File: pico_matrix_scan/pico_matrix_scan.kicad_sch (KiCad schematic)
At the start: 8 parts, among them SW1 SW_Reed, SW2 SW_Reed, SW3 SW_Reed, SW4 SW_Reed

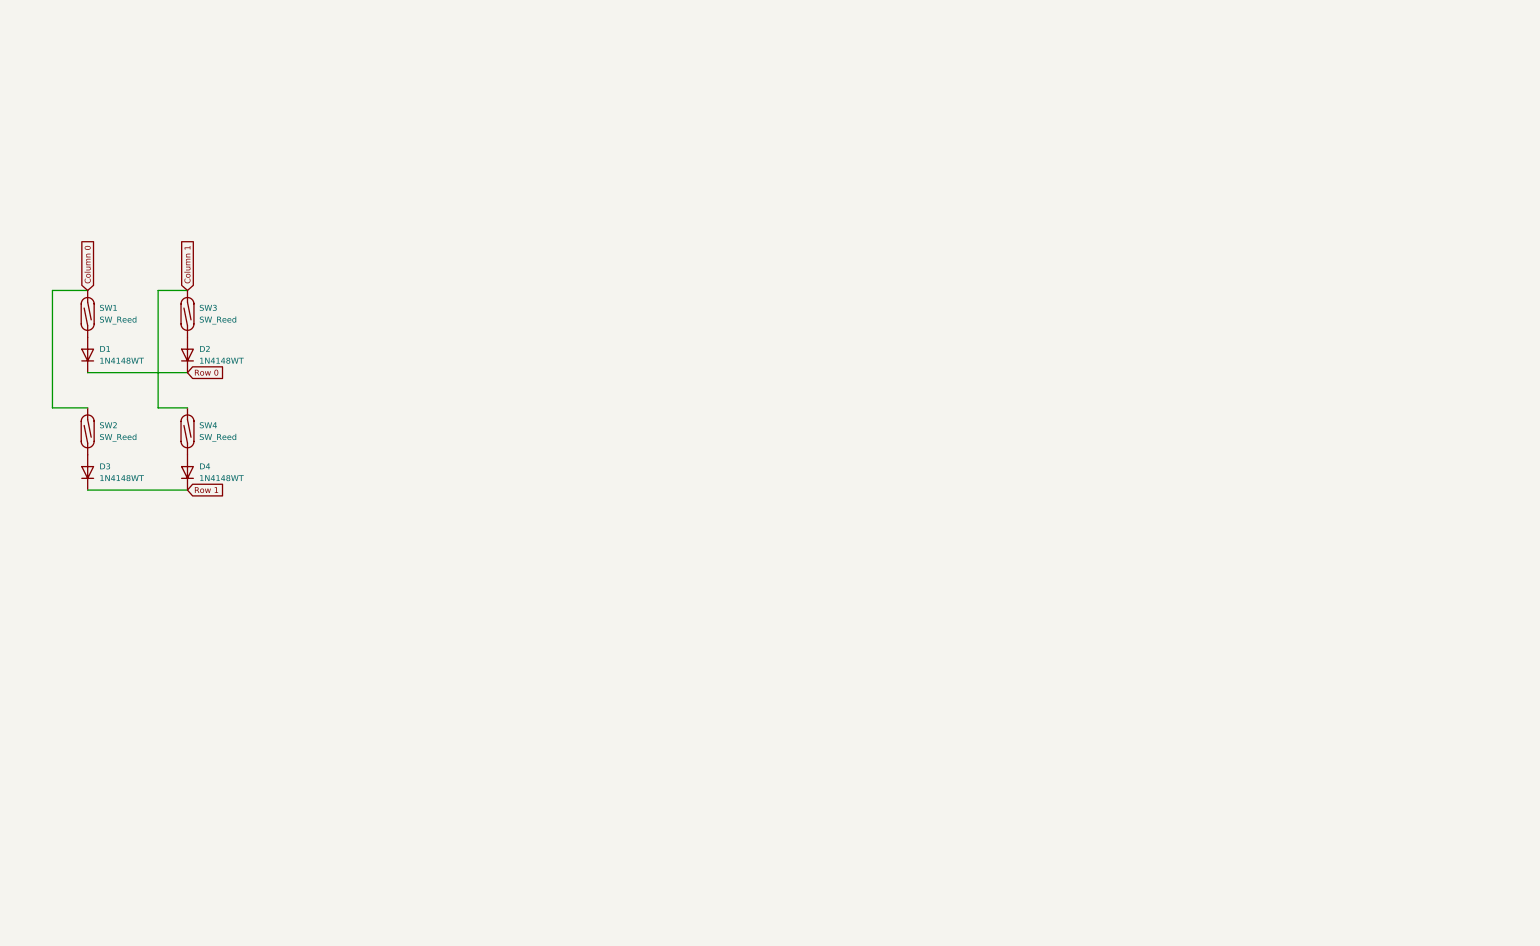
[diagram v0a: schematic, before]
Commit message: Create full-size schematic
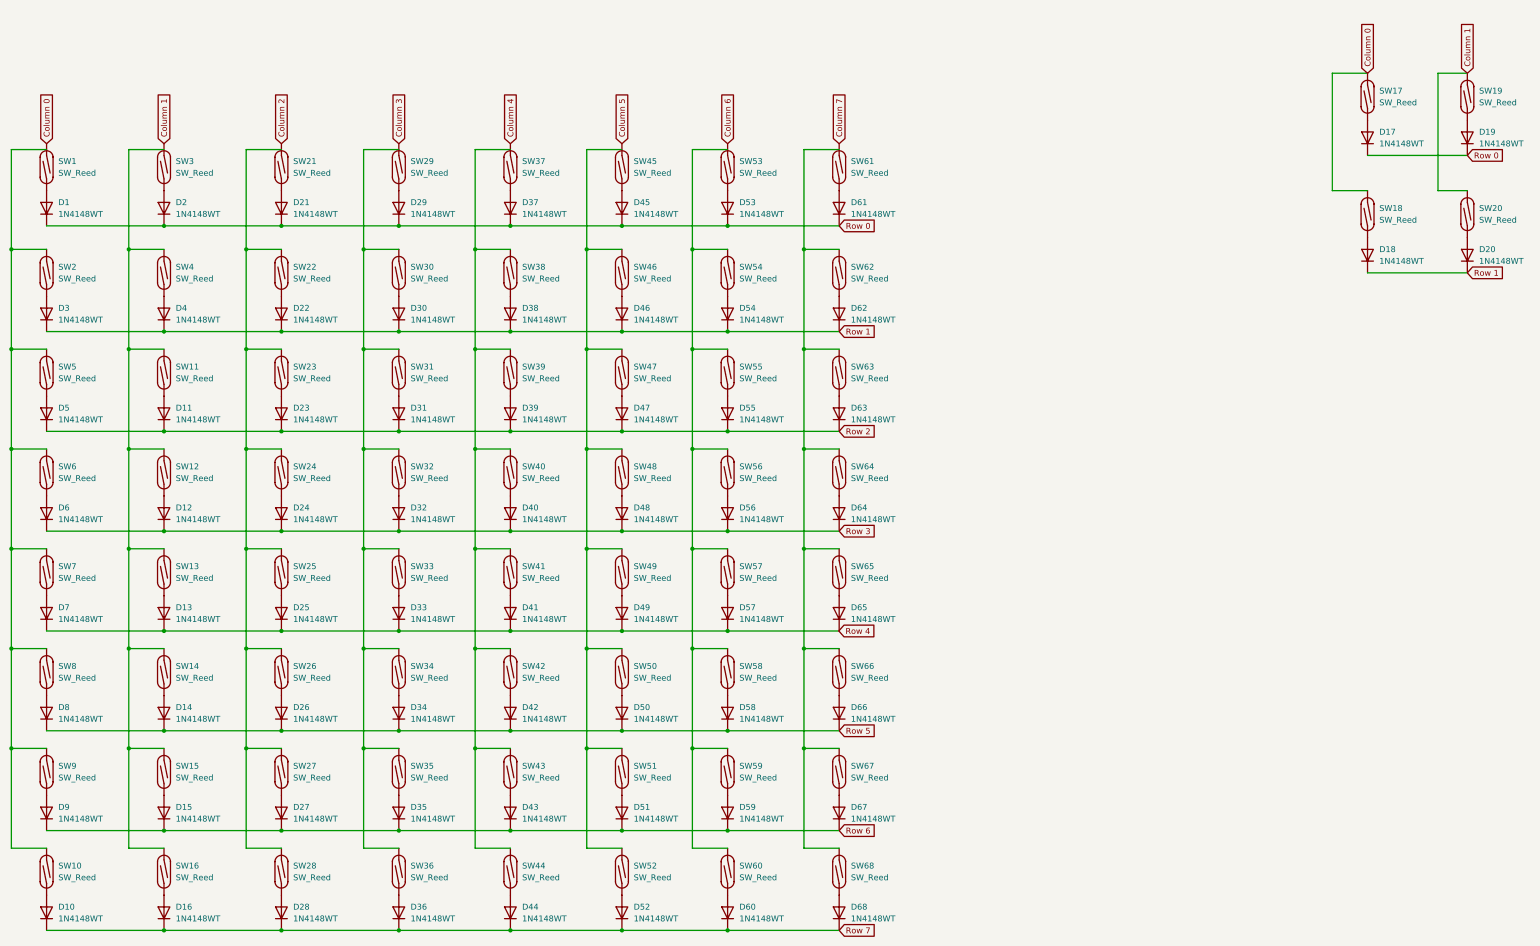
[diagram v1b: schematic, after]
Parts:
- added D10, D11, D12, D13, D14, D15, D16, D17, D18, D19, D20, D21, D22, D23, D24, D25, D26, D27, D28, D29, D30, D31, D32, D33, D34, D35, D36, D37, D38, D39, D40, D41, D42, D43, D44, D45, D46, D47, D48, D49, D5, D50, D51, D52, D53, D54, D55, D56, D57, D58, D59, D6, D60, D61, D62, D63, D64, D65, D66, D67, D68, D7, D8, D9: 1N4148WT, Diode_SMD:D_SOD-523, symbol Diode:1N4148WT
- added SW10, SW11, SW12, SW13, SW14, SW15, SW16, SW17, SW18, SW19, SW20, SW21, SW22, SW23, SW24, SW25, SW26, SW27, SW28, SW29, SW30, SW31, SW32, SW33, SW34, SW35, SW36, SW37, SW38, SW39, SW40, SW41, SW42, SW43, SW44, SW45, SW46, SW47, SW48, SW49, SW5, SW50, SW51, SW52, SW53, SW54, SW55, SW56, SW57, SW58, SW59, SW6, SW60, SW61, SW62, SW63, SW64, SW65, SW66, SW67, SW68, SW7, SW8, SW9: SW_Reed, symbol Switch:SW_Reed
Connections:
- net Column 0: now also SW17.2, SW18.2; no longer SW2.2
- net Column 1: now also SW19.2, SW20.2; no longer SW4.2
- net Row 0: now also D17.1 (K), D19.1 (K), D21.1 (K), D29.1 (K), D37.1 (K), D45.1 (K), D53.1 (K), D61.1 (K)
- net Row 1: now also D18.1 (K), D20.1 (K), D22.1 (K), D30.1 (K), D38.1 (K), D46.1 (K), D54.1 (K), D62.1 (K)
- new net: D45.2 (A), SW45.1
- new net: D9.2 (A), SW9.1
- new net: SW10.2, SW2.2, SW5.2, SW6.2, SW7.2, SW8.2, SW9.2
- new net: D20.2 (A), SW20.1
- new net: D24.2 (A), SW24.1
- new net: D5.2 (A), SW5.1
- new net: D59.2 (A), SW59.1
- new net: D56.2 (A), SW56.1
- new net: SW54.2, SW55.2, SW56.2, SW57.2, SW58.2, SW59.2, SW60.2
- new net: D34.2 (A), SW34.1
- new net: SW30.2, SW31.2, SW32.2, SW33.2, SW34.2, SW35.2, SW36.2
- new net: SW11.2, SW12.2, SW13.2, SW14.2, SW15.2, SW16.2, SW4.2
- new net: D38.2 (A), SW38.1
- new net: SW38.2, SW39.2, SW40.2, SW41.2, SW42.2, SW43.2, SW44.2
- new net: D51.2 (A), SW51.1
- new net: D13.2 (A), SW13.1
- new net: D30.2 (A), SW30.1
- new net: D46.2 (A), SW46.1
- new net: SW46.2, SW47.2, SW48.2, SW49.2, SW50.2, SW51.2, SW52.2
- new net: D63.2 (A), SW63.1
- new net: D25.2 (A), SW25.1
- new net: SW22.2, SW23.2, SW24.2, SW25.2, SW26.2, SW27.2, SW28.2
- new net: D43.2 (A), SW43.1
- new net: D48.2 (A), SW48.1
- new net: D35.2 (A), SW35.1
- new net: D64.2 (A), SW64.1
- new net: SW62.2, SW63.2, SW64.2, SW65.2, SW66.2, SW67.2, SW68.2
- new net: D15.2 (A), SW15.1
- new net: D52.2 (A), SW52.1
- new net: D21.2 (A), SW21.1
- new net: D8.2 (A), SW8.1
- new net: D23.2 (A), SW23.1
- new net: D42.2 (A), SW42.1
- new net: D19.2 (A), SW19.1
- new net: D67.2 (A), SW67.1
- new net: D36.2 (A), SW36.1
- new net: D39.2 (A), SW39.1
- new net: D41.2 (A), SW41.1
- new net: D61.2 (A), SW61.1
- new net: D11.2 (A), SW11.1
- new net: D50.2 (A), SW50.1
- new net: D57.2 (A), SW57.1
- new net: D49.2 (A), SW49.1
- new net: D33.2 (A), SW33.1
- new net: D60.2 (A), SW60.1
- new net: D62.2 (A), SW62.1
- new net: D14.2 (A), SW14.1
- new net: D47.2 (A), SW47.1
- new net: D7.2 (A), SW7.1
- new net: D10.2 (A), SW10.1
- new net: D37.2 (A), SW37.1
- new net: D31.2 (A), SW31.1
- new net: D54.2 (A), SW54.1
- new net: D55.2 (A), SW55.1
- new net: D40.2 (A), SW40.1
- new net: D6.2 (A), SW6.1
- new net: D17.2 (A), SW17.1
- new net: D29.2 (A), SW29.1
- new net: D68.2 (A), SW68.1
- new net: D12.2 (A), SW12.1
- new net: D32.2 (A), SW32.1
- new net: D22.2 (A), SW22.1
- new net: D44.2 (A), SW44.1
- new net: D18.2 (A), SW18.1
- new net: D27.2 (A), SW27.1
- new net: D16.2 (A), SW16.1
- new net: D65.2 (A), SW65.1
- new net: D26.2 (A), SW26.1
- new net: D58.2 (A), SW58.1
- new net: D66.2 (A), SW66.1
- new net: D28.2 (A), SW28.1
- new net: D53.2 (A), SW53.1
- new net Column 2: SW21.2
- new net Column 3: SW29.2
- new net Column 4: SW37.2
- new net Column 5: SW45.2
- new net Column 6: SW53.2
- new net Column 7: SW61.2
- new net Row 2: D11.1 (K), D23.1 (K), D31.1 (K), D39.1 (K), D47.1 (K), D5.1 (K), D55.1 (K), D63.1 (K)
- new net Row 3: D12.1 (K), D24.1 (K), D32.1 (K), D40.1 (K), D48.1 (K), D56.1 (K), D6.1 (K), D64.1 (K)
- new net Row 4: D13.1 (K), D25.1 (K), D33.1 (K), D41.1 (K), D49.1 (K), D57.1 (K), D65.1 (K), D7.1 (K)
- new net Row 5: D14.1 (K), D26.1 (K), D34.1 (K), D42.1 (K), D50.1 (K), D58.1 (K), D66.1 (K), D8.1 (K)
- new net Row 6: D15.1 (K), D27.1 (K), D35.1 (K), D43.1 (K), D51.1 (K), D59.1 (K), D67.1 (K), D9.1 (K)
- new net Row 7: D10.1 (K), D16.1 (K), D28.1 (K), D36.1 (K), D44.1 (K), D52.1 (K), D60.1 (K), D68.1 (K)
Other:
- moved on the sheet: D1, D3, SW1, SW2

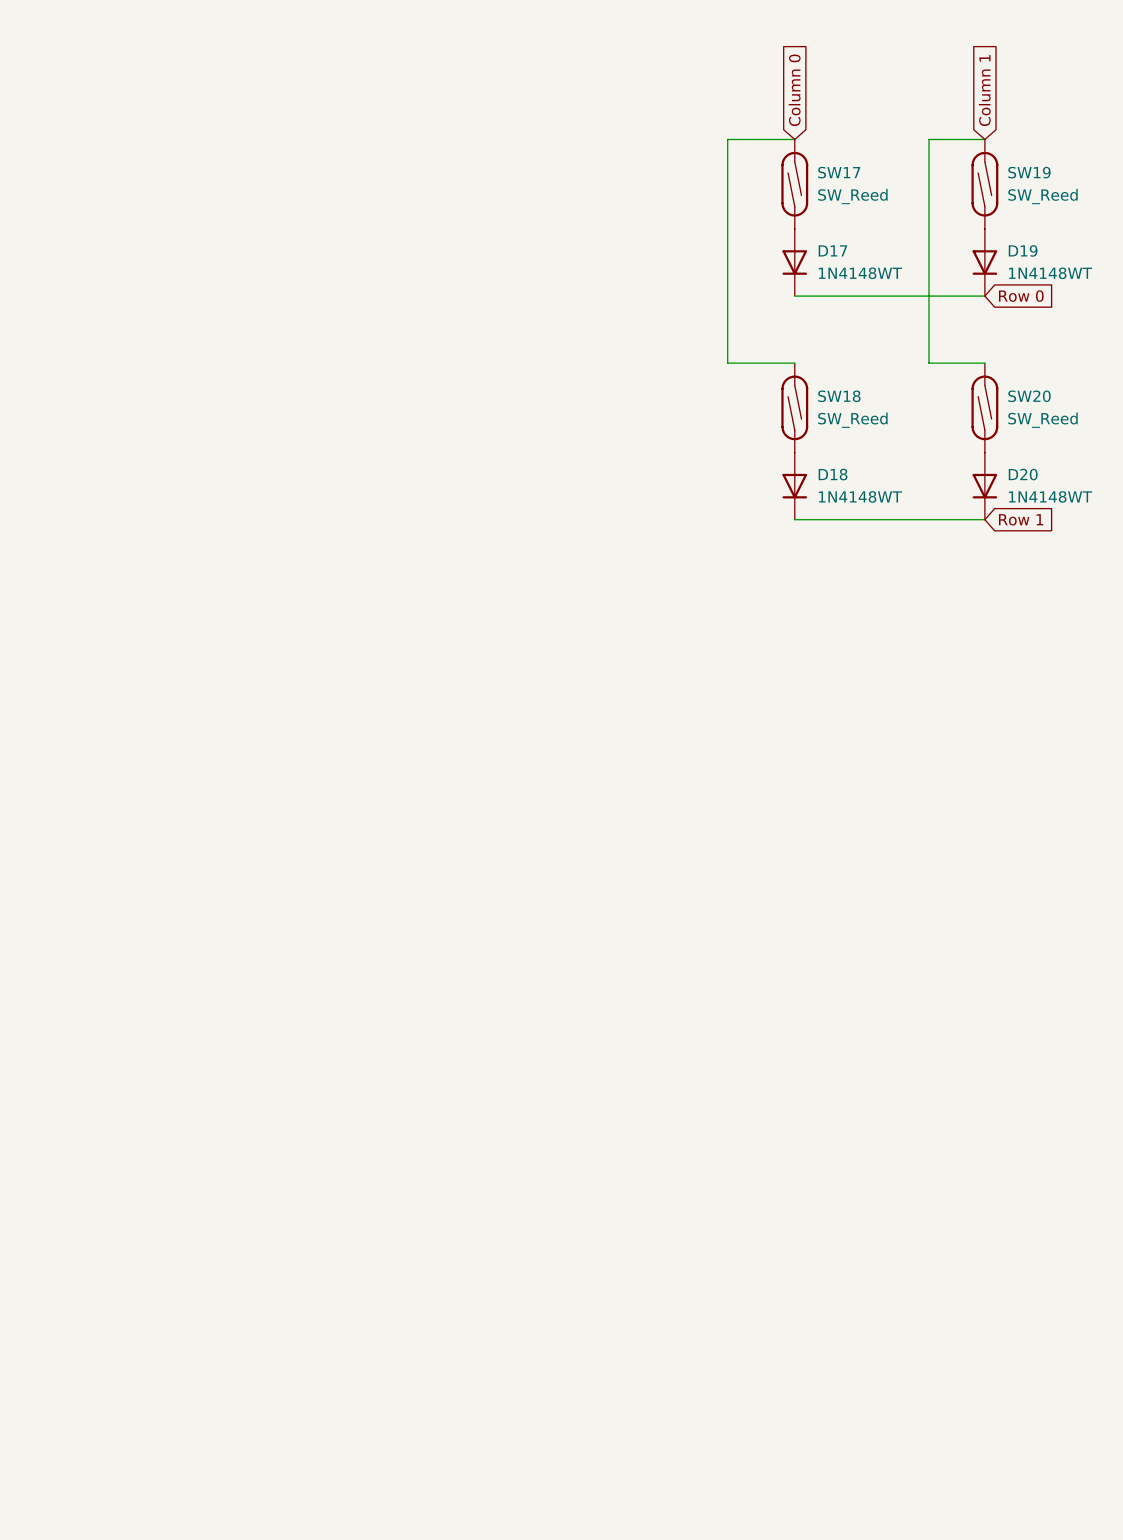
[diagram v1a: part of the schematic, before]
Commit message: Add Pico to KiCAD schematic
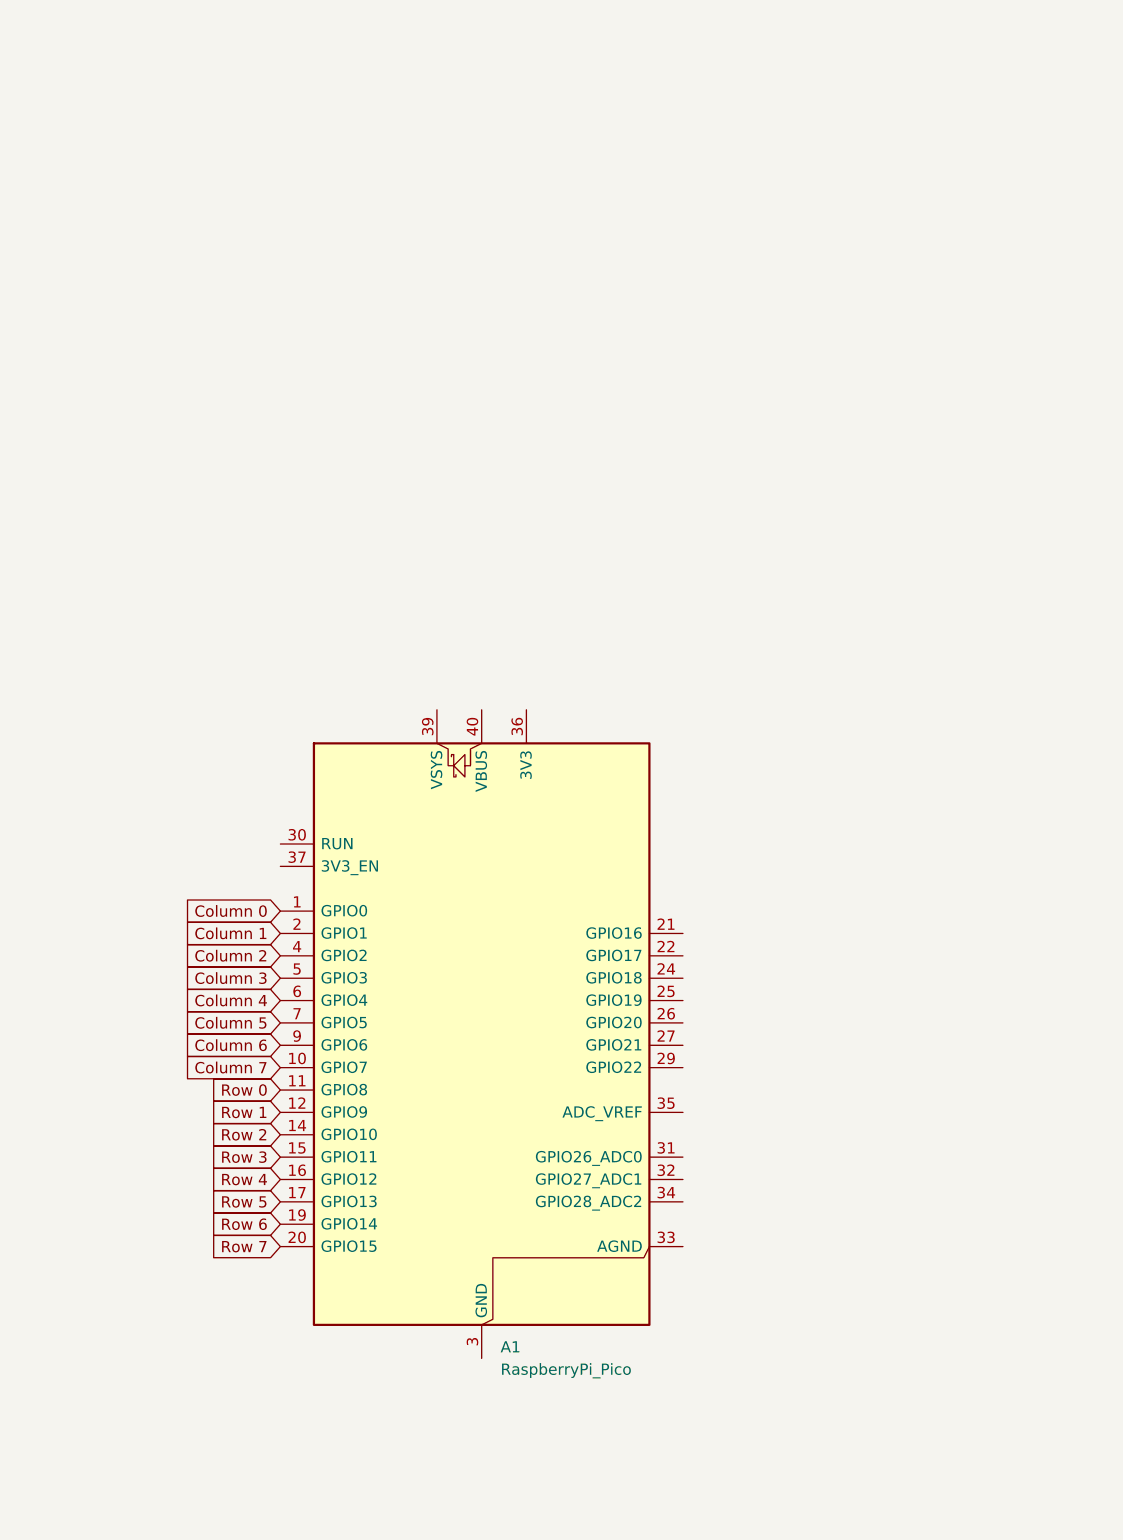
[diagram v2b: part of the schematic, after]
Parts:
- removed D17, D18, D19, D20: 1N4148WT, Diode_SMD:D_SOD-523, symbol Diode:1N4148WT
- removed SW17, SW18, SW19, SW20: SW_Reed, symbol Switch:SW_Reed
- added A1: RaspberryPi_Pico, Module:RaspberryPi_Pico_Common_Unspecified, symbol MCU_Module:RaspberryPi_Pico
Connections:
- net Column 0: now also A1.1 (GPIO0)
- net Column 1: now also A1.2 (GPIO1)
- net Column 2: now also A1.4 (GPIO2)
- net Column 3: now also A1.5 (GPIO3)
- net Column 4: now also A1.6 (GPIO4)
- net Column 5: now also A1.7 (GPIO5)
- net Column 6: now also A1.9 (GPIO6)
- net Column 7: now also A1.10 (GPIO7)
- net Row 0: now also A1.11 (GPIO8)
- net Row 1: now also A1.12 (GPIO9)
- net Row 2: now also A1.14 (GPIO10)
- net Row 3: now also A1.15 (GPIO11)
- net Row 4: now also A1.16 (GPIO12)
- net Row 5: now also A1.17 (GPIO13)
- net Row 6: now also A1.19 (GPIO14)
- net Row 7: now also A1.20 (GPIO15)
- new net: A1.13 (GND), A1.18 (GND), A1.23 (GND), A1.28 (GND), A1.3 (GND), A1.38 (GND), A1.8 (GND)
